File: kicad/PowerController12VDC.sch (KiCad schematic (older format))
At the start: 0 parts

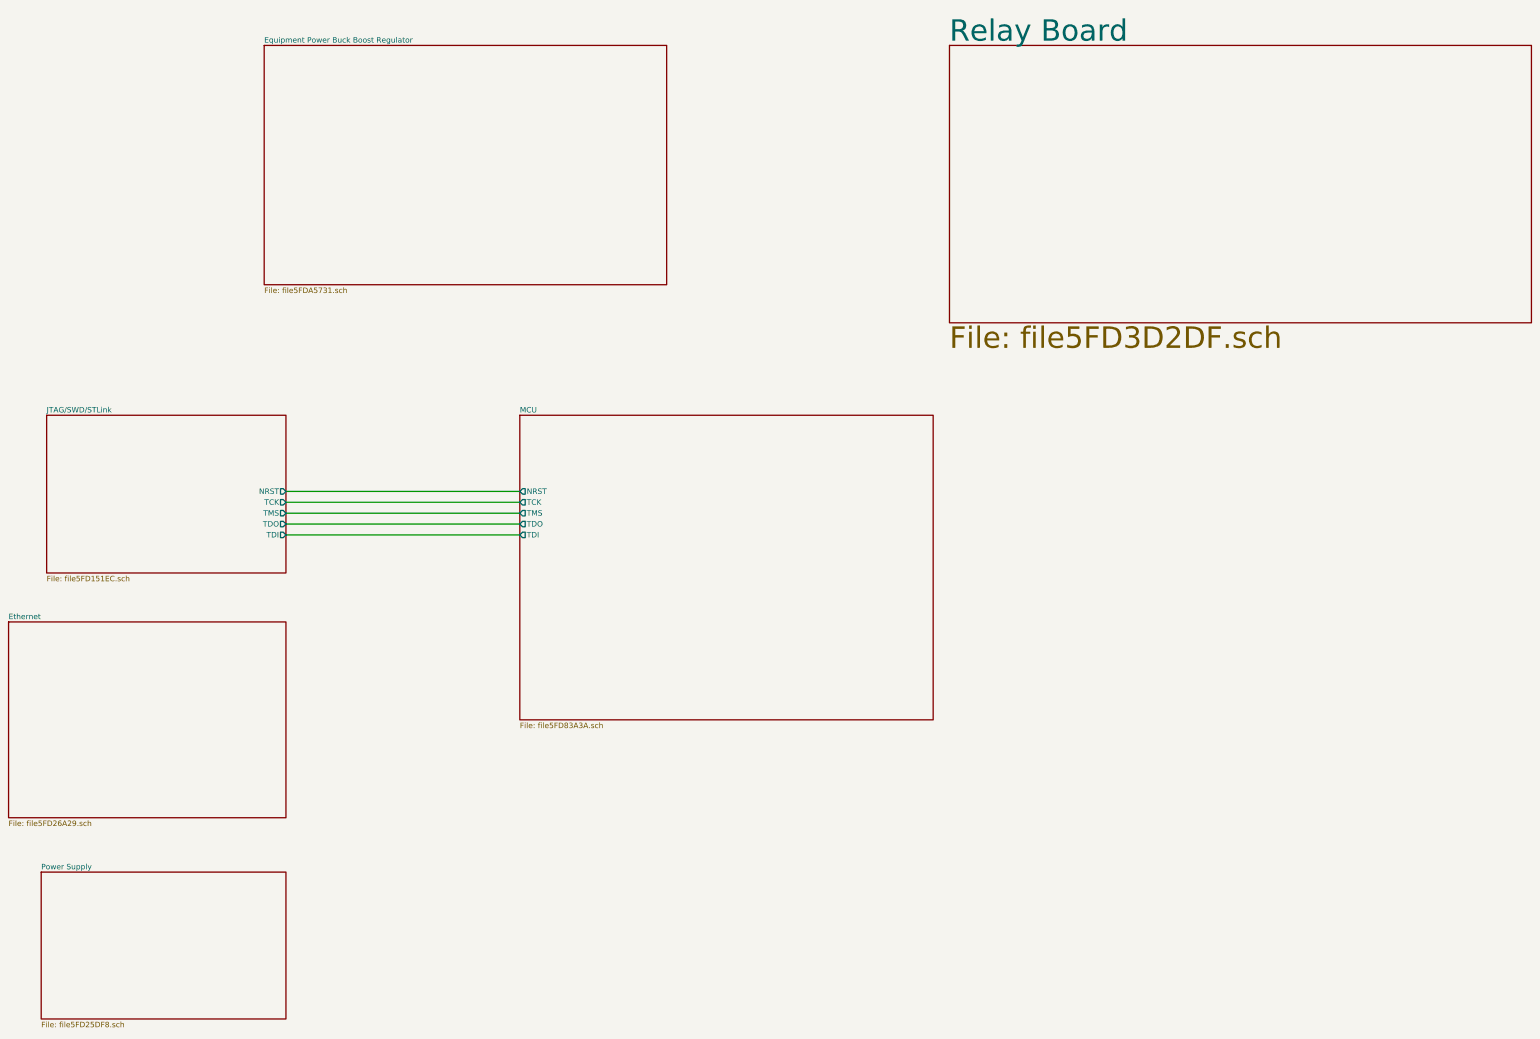
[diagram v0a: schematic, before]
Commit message: Adjust component values for 13.8V; add RUNSTOP driver
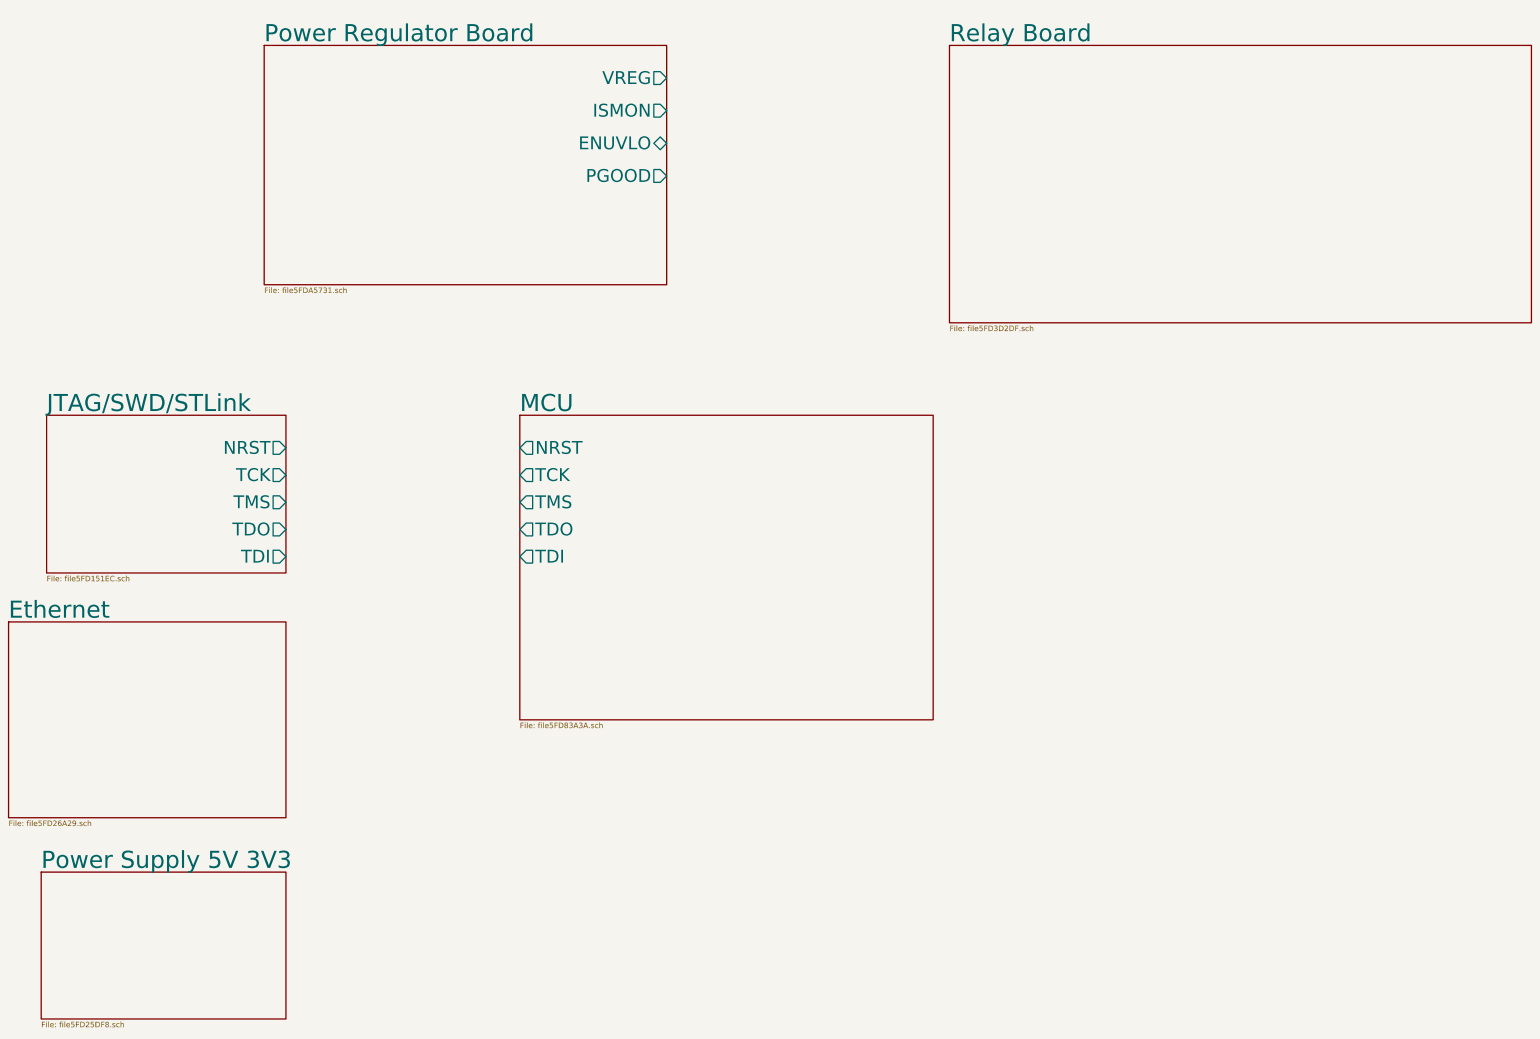
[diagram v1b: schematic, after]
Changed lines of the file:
@@
 S 2450 8650 2250 1350
 U 5FD25DF9
-F0 "Power Supply" 50
+F0 "Power Supply 5V 3V3" 157
 F1 "file5FD25DF8.sch" 50
 $EndSheet
@@
 S 6850 4450 3800 2800
 U 5FD83A3B
-F0 "MCU" 50
+F0 "MCU" 157
 F1 "file5FD83A3A.sch" 50
-F2 "TMS" O L 6850 5350 50
-F3 "TCK" O L 6850 5250 50
-F4 "TDI" O L 6850 5550 50
-F5 "TDO" O L 6850 5450 50
-F6 "NRST" O L 6850 5150 50
+F2 "TMS" O L 6850 5250 118
+F3 "TCK" O L 6850 5000 118
+F4 "TDI" O L 6850 5750 118
+F5 "TDO" O L 6850 5500 118
+F6 "NRST" O L 6850 4750 118
 $EndSheet
-Wire Wire Line
-	4700 5150 6850 5150
-Wire Wire Line
-	4700 5250 6850 5250
-Wire Wire Line
-	4700 5350 6850 5350
-Wire Wire Line
-	4700 5450 6850 5450
-Wire Wire Line
-	4700 5550 6850 5550
 $Sheet
 S 2150 6350 2550 1800
 U 5FD26A2A
-F0 "Ethernet" 50
+F0 "Ethernet" 157
 F1 "file5FD26A29.sch" 50
 $EndSheet
@@
 S 10800 1050 5350 2550
 U 5FD3D2E0
-F0 "Relay Board" 197
-F1 "file5FD3D2DF.sch" 197
+F0 "Relay Board" 157
+F1 "file5FD3D2DF.sch" 50
 $EndSheet
 $Sheet
 S 2500 4450 2200 1450
 U 5FD151ED
-F0 "JTAG/SWD/STLink" 50
+F0 "JTAG/SWD/STLink" 157
 F1 "file5FD151EC.sch" 50
-F2 "NRST" O R 4700 5150 50
-F3 "TCK" O R 4700 5250 50
-F4 "TMS" O R 4700 5350 50
-F5 "TDO" O R 4700 5450 50
-F6 "TDI" O R 4700 5550 50
+F2 "NRST" O R 4700 4750 118
+F3 "TCK" O R 4700 5000 118
+F4 "TMS" O R 4700 5250 118
+F5 "TDO" O R 4700 5500 118
+F6 "TDI" O R 4700 5750 118
 $EndSheet
 $Sheet
 S 4500 1050 3700 2200
 U 5FDA5732
-F0 "Equipment Power Buck Boost Regulator" 50
+F0 "Power Regulator Board" 157
 F1 "file5FDA5731.sch" 50
+F2 "PGOOD" O R 8200 2250 118
+F3 "ENUVLO" B R 8200 1950 118
+F4 "VREG" O R 8200 1350 118
+F5 "ISMON" O R 8200 1650 118
 $EndSheet
 $EndSCHEMATC

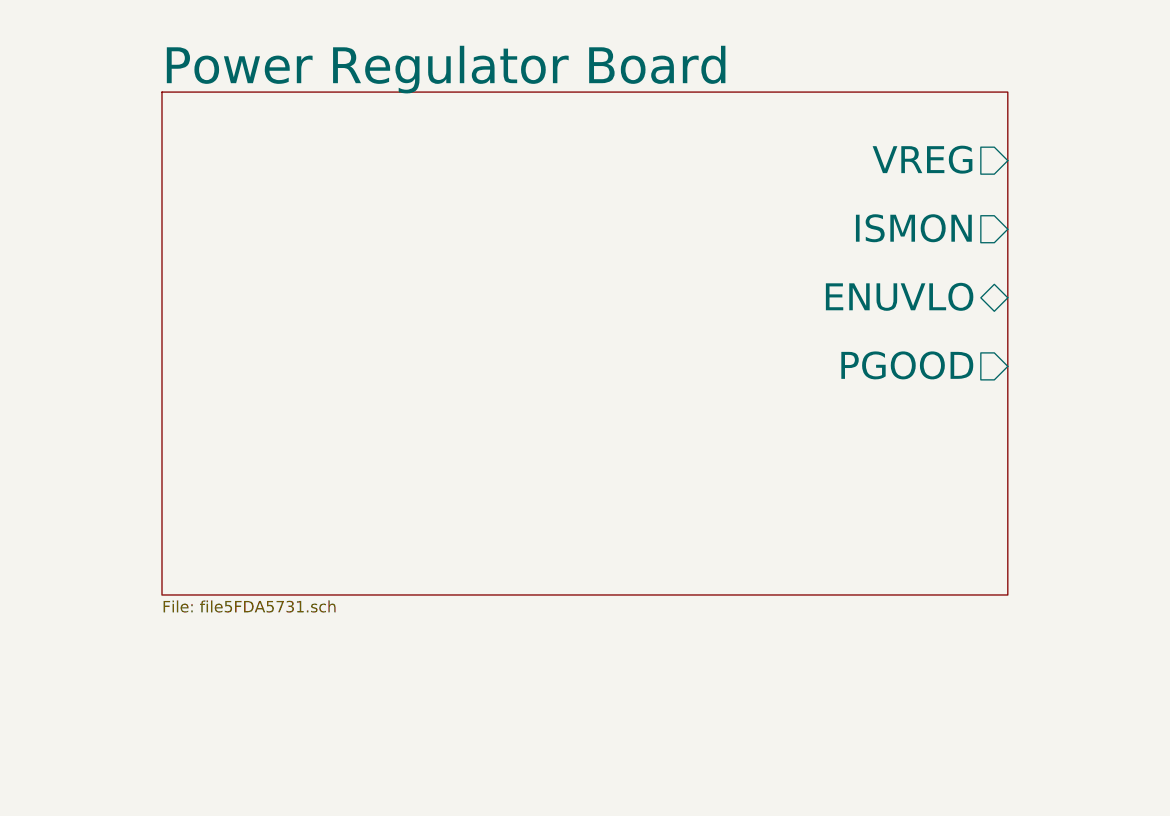
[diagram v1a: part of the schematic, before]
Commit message: Jumpers for power reg int/ext voltage control
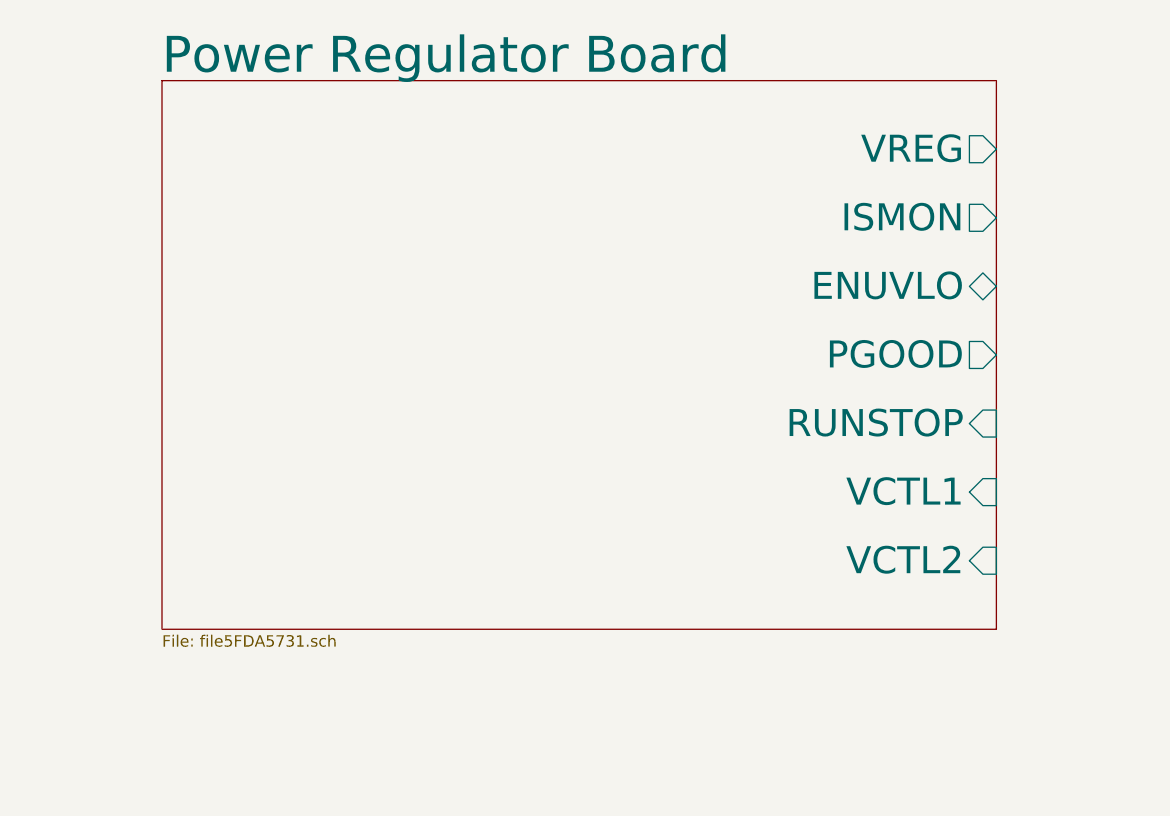
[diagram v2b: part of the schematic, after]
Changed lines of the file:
@@
 $EndSheet
 $Sheet
-S 4500 1050 3700 2200
+S 4500 1000 3650 2400
 U 5FDA5732
 F0 "Power Regulator Board" 157
 F1 "file5FDA5731.sch" 50
-F2 "PGOOD" O R 8200 2250 118
-F3 "ENUVLO" B R 8200 1950 118
-F4 "VREG" O R 8200 1350 118
-F5 "ISMON" O R 8200 1650 118
+F2 "PGOOD" O R 8150 2200 118
+F3 "ENUVLO" B R 8150 1900 118
+F4 "VREG" O R 8150 1300 118
+F5 "ISMON" O R 8150 1600 118
+F6 "RUNSTOP" I R 8150 2500 118
+F7 "VCTL1" I R 8150 2800 118
+F8 "VCTL2" I R 8150 3100 118
 $EndSheet
 $EndSCHEMATC

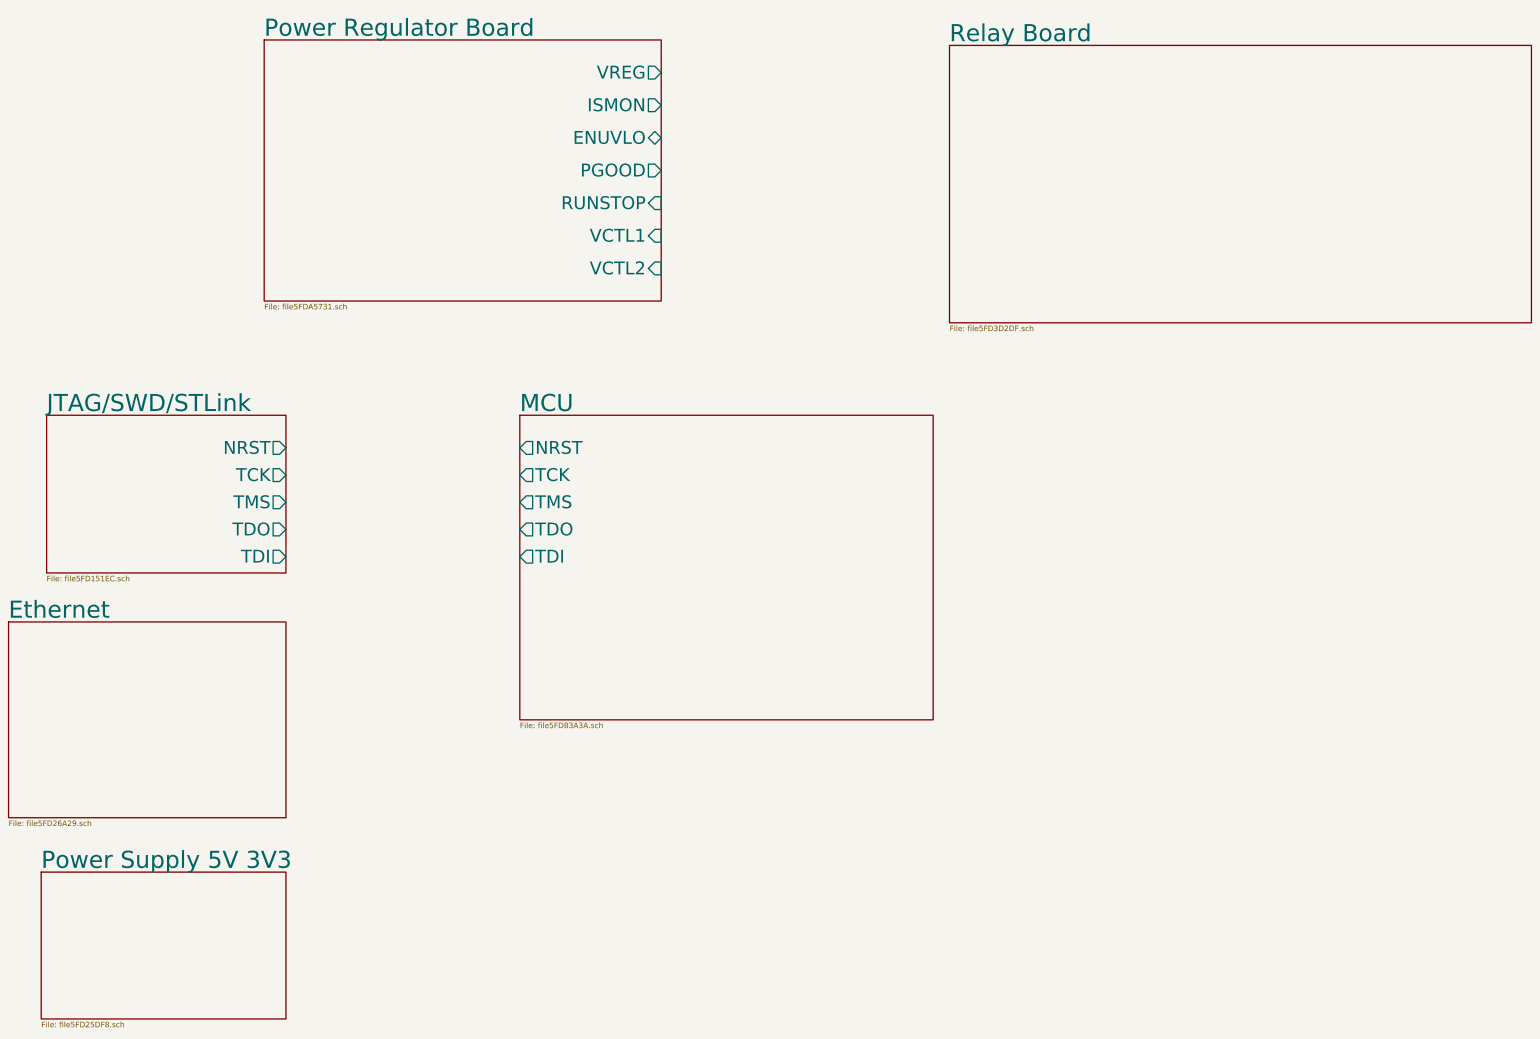
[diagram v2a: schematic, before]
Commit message: Ethernet initial schematic; start ERC
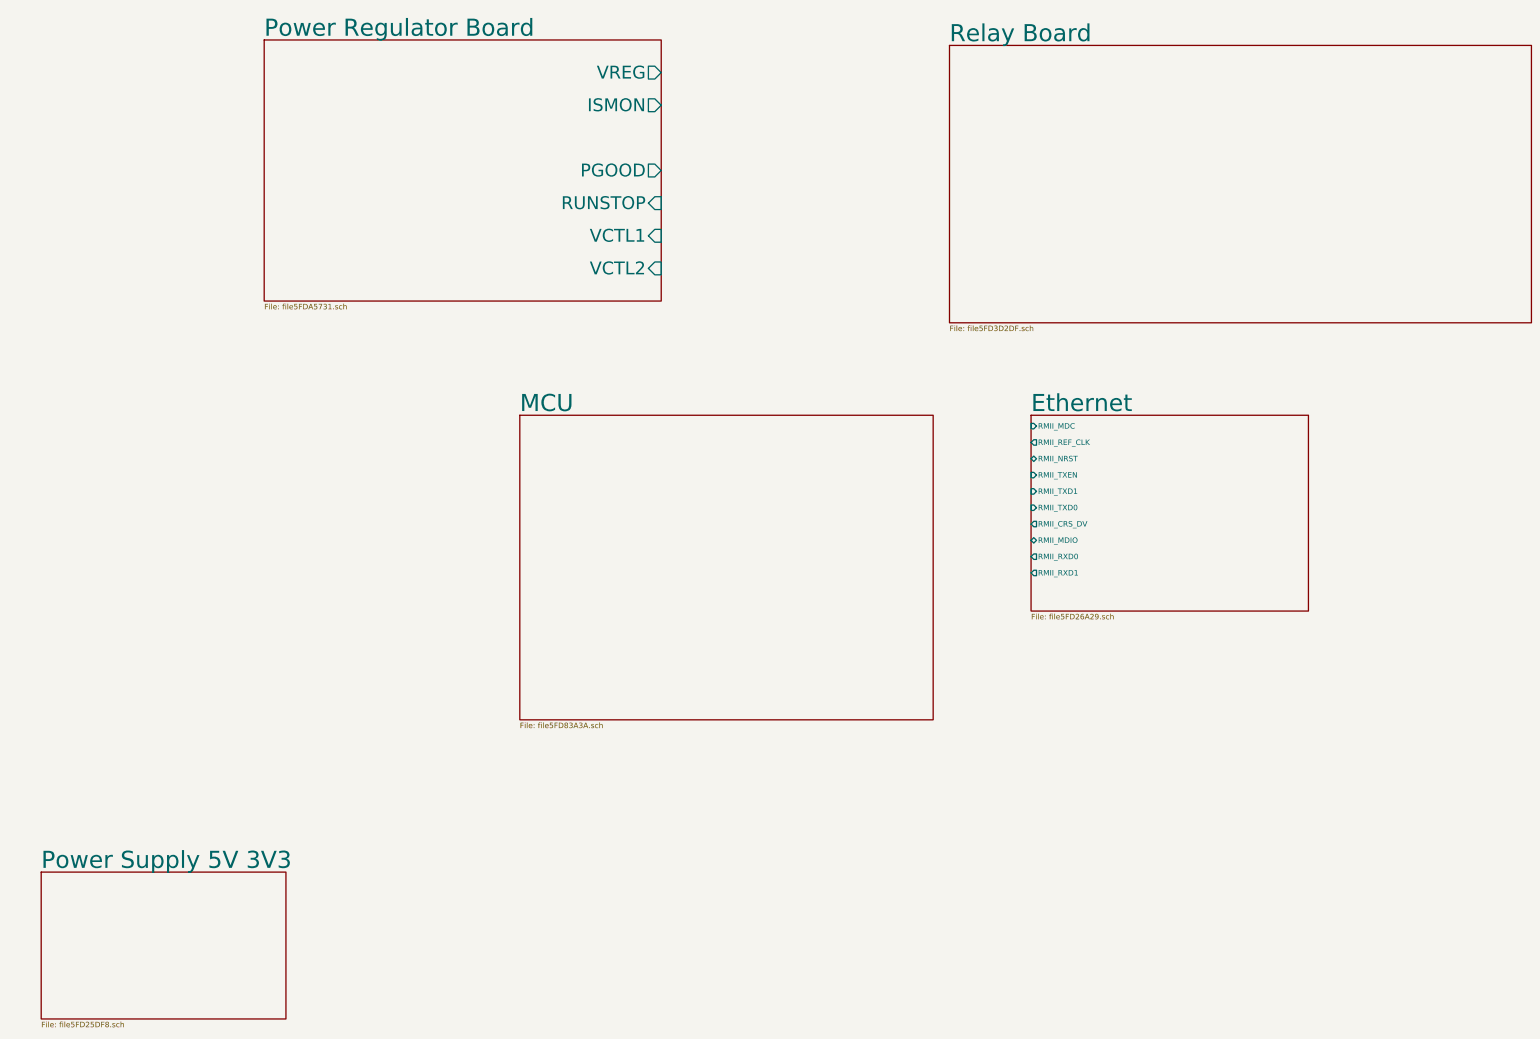
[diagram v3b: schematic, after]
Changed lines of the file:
@@
 $Descr USLedger 17000 11000
 encoding utf-8
-Sheet 1 7
+Sheet 1 6
 Title "KQ9P Power Controller 12VDC"
 Date "2020-12-08"
@@
 F0 "MCU" 157
 F1 "file5FD83A3A.sch" 50
-F2 "TMS" O L 6850 5250 118
-F3 "TCK" O L 6850 5000 118
-F4 "TDI" O L 6850 5750 118
-F5 "TDO" O L 6850 5500 118
-F6 "NRST" O L 6850 4750 118
 $EndSheet
 $Sheet
-S 2150 6350 2550 1800
+S 11550 4450 2550 1800
 U 5FD26A2A
 F0 "Ethernet" 157
 F1 "file5FD26A29.sch" 50
+F2 "RMII_TXD0" I L 11550 5300 50
+F3 "RMII_TXD1" I L 11550 5150 50
+F4 "RMII_TXEN" I L 11550 5000 50
+F5 "RMII_NRST" B L 11550 4850 50
+F6 "RMII_REF_CLK" O L 11550 4700 50
+F7 "RMII_MDC" I L 11550 4550 50
+F8 "RMII_CRS_DV" O L 11550 5450 50
+F9 "RMII_MDIO" B L 11550 5600 50
+F10 "RMII_RXD0" O L 11550 5750 50
+F11 "RMII_RXD1" O L 11550 5900 50
 $EndSheet
 $Sheet
@@
 $EndSheet
 $Sheet
-S 2500 4450 2200 1450
-U 5FD151ED
-F0 "JTAG/SWD/STLink" 157
-F1 "file5FD151EC.sch" 50
-F2 "NRST" O R 4700 4750 118
-F3 "TCK" O R 4700 5000 118
-F4 "TMS" O R 4700 5250 118
-F5 "TDO" O R 4700 5500 118
-F6 "TDI" O R 4700 5750 118
-$EndSheet
-$Sheet
 S 4500 1000 3650 2400
 U 5FDA5732
@@
 F1 "file5FDA5731.sch" 50
 F2 "PGOOD" O R 8150 2200 118
-F3 "ENUVLO" B R 8150 1900 118
-F4 "VREG" O R 8150 1300 118
-F5 "ISMON" O R 8150 1600 118
-F6 "RUNSTOP" I R 8150 2500 118
-F7 "VCTL1" I R 8150 2800 118
-F8 "VCTL2" I R 8150 3100 118
+F3 "VREG" O R 8150 1300 118
+F4 "ISMON" O R 8150 1600 118
+F5 "RUNSTOP" I R 8150 2500 118
+F6 "VCTL1" I R 8150 2800 118
+F7 "VCTL2" I R 8150 3100 118
 $EndSheet
 $EndSCHEMATC
